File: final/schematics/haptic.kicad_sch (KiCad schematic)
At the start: 11 parts, among them U4 DRV2605LDGST, U5 DRV2605LDGST, U6 DRV2605LDGST

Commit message: fixing issues
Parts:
- C10, C11, C12, C5, C6, C7, C8, C9: footprint (none) -> Capacitor_SMD:C_0603_1608Metric
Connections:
- net +3V3: no longer C10.1, C12.1, C7.1, U4.10 (VDD), U4.5 (EN), U5.10 (VDD), U5.5 (EN), U6.10 (VDD), U6.5 (EN)
- new net +3V3D: C10.1, C12.1, C7.1, U4.10 (VDD), U4.5 (EN), U5.10 (VDD), U5.5 (EN), U6.10 (VDD), U6.5 (EN)

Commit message: finishing
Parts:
- added C39, C41: 10uF, Capacitor_SMD:C_0603_1608Metric, symbol Device:C
- added C40, C42: 0.1uF, Capacitor_SMD:C_0603_1608Metric, symbol Device:C
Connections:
- net +3V3 is gone; now on net +3V3D: C5.1, C6.1
- net +3V3D: now also C39.1, C40.1, C41.1, C42.1
- net DGND: now also C39.2, C40.2, C41.2, C42.2
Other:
- note added: "Decoupling"
- moved on the sheet: C10, C11, C12, C5, C6, C7, C8, C9, U4, U5, U6

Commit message: finished
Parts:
- removed C11, C12: 1uF, Capacitor_SMD:C_0603_1608Metric, symbol Device:C
- removed C41: 10uF, Capacitor_SMD:C_0603_1608Metric, symbol Device:C
- removed C42: 0.1uF, Capacitor_SMD:C_0603_1608Metric, symbol Device:C
- removed U6: DRV2605LDGST, DRV2605LDGST:SOP50P490X110-10N, symbol DRV2605LDGST:DRV2605LDGST
- added R42, R43, R44, R45: 2.2k, Resistor_SMD:R_0603_1608Metric, symbol Device:R
- added R46, R47, R48: 10k, Resistor_SMD:R_0603_1608Metric, symbol Device:R
- added TP17, TP18: TestPoint, Connector_Pin:Pin_D1.0mm_L10.0mm_LooseFit, symbol Connector:TestPoint
- added TP19: MOT1+, Connector_Pin:Pin_D1.1mm_L8.5mm_W2.5mm_FlatFork, symbol Connector:TestPoint
- added TP20: MOT1-, Connector_Pin:Pin_D1.1mm_L8.5mm_W2.5mm_FlatFork, symbol Connector:TestPoint
- added TP21: MOT2+, Connector_Pin:Pin_D1.1mm_L8.5mm_W2.5mm_FlatFork, symbol Connector:TestPoint
- added TP22: MOT2-, Connector_Pin:Pin_D1.1mm_L8.5mm_W2.5mm_FlatFork, symbol Connector:TestPoint
- added U3: TCA9543APWR, TCA9543APWR:IC_TCA9543APWR, symbol TCA9543APWR:TCA9543APWR
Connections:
- net +3V3D: now also R42.2, R43.2, R44.2, R45.2, R46.1, R47.1, R48.1, U3.14 (VCC)
- net DGND: now also U3.1 (A0), U3.2 (A1), U3.7 (GND)
- net MOT1+: now also TP19.1
- net MOT1-: now also TP20.1
- net MOT2+: now also TP21.1
- net MOT2-: now also TP22.1
- net PWM1: now also TP17.1
- net PWM2: now also TP18.1
- net SCL: now also U3.12 (SCL)
- net SDA: now also U3.13 (SDA)
- new net: R46.2, U3.4 (~{INT0})
- new net: R47.2, U3.8 (~{INT1})
- new net: R42.1, U3.10 (SC1)
- new net: R48.2, U3.3 (~{RESET})
- new net: R45.1, U3.5 (SD0)
- new net: R44.1, U3.6 (SC0)
- new net: R43.1, U3.9 (SD1)
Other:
- note removed: "Haptic Driver 3"
- moved on the sheet: C39, C40, C5, C6

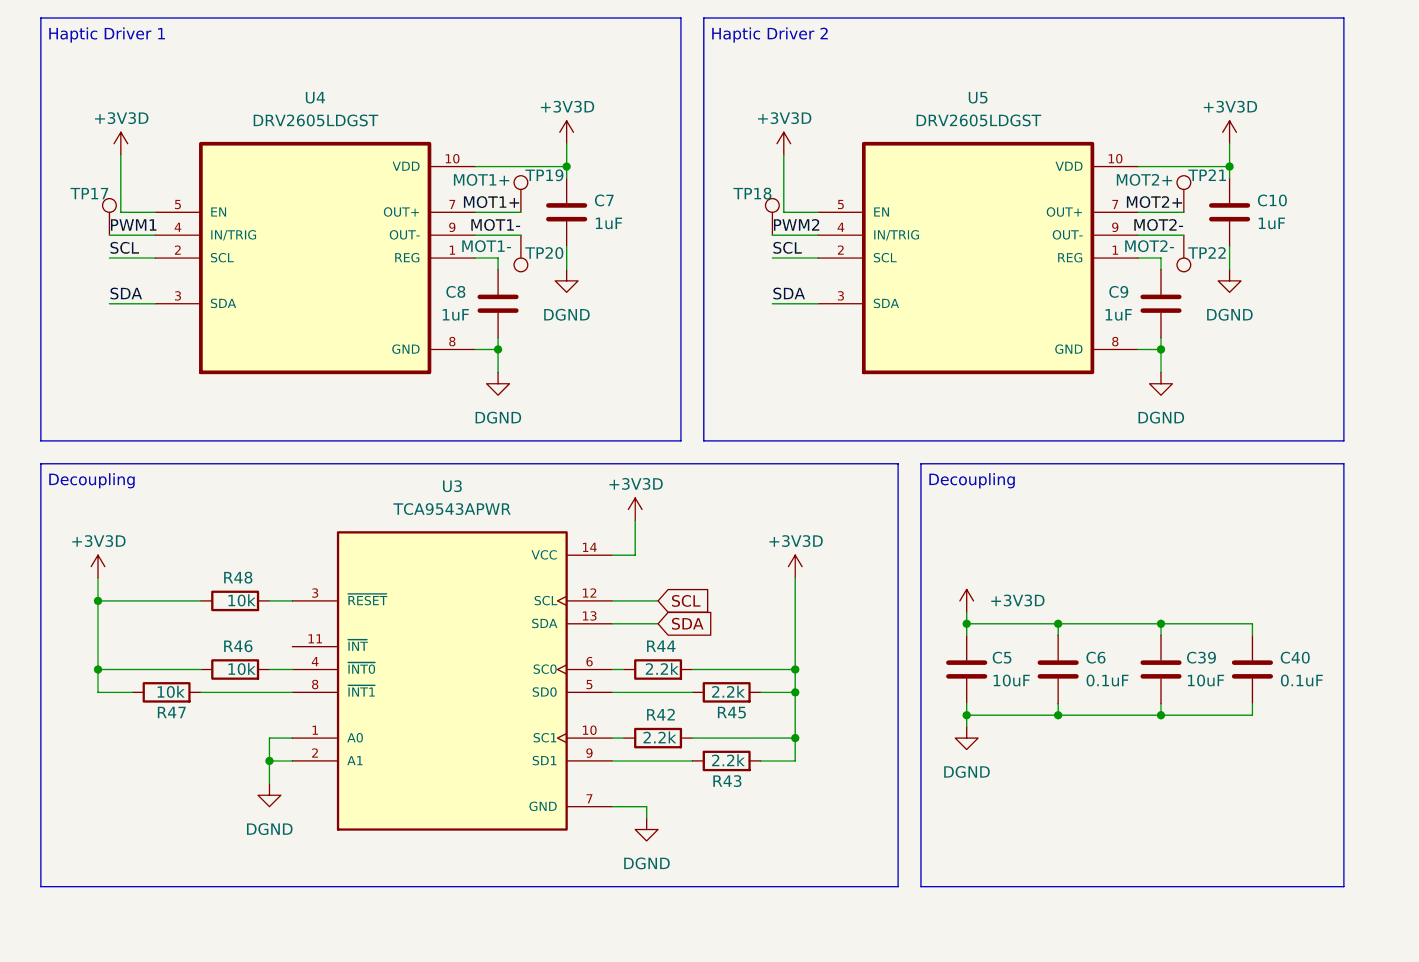
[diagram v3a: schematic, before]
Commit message: fixed jumper connection
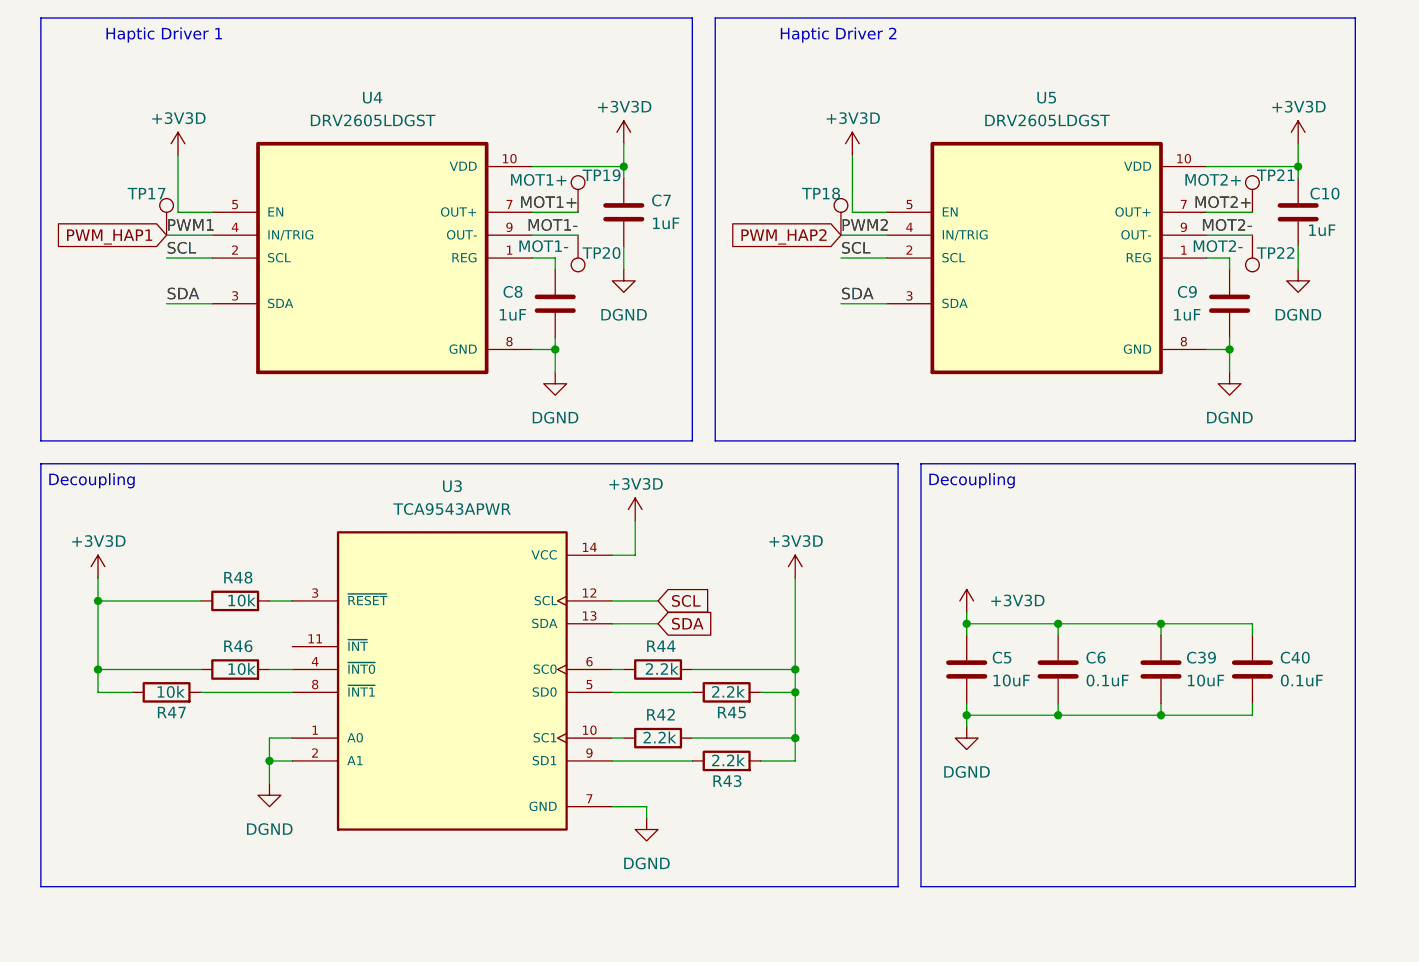
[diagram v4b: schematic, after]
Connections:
- net PWM1 renamed PWM_HAP1
- net PWM2 renamed PWM_HAP2
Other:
- moved on the sheet: C10, C7, C8, C9, TP17, TP18, TP19, TP20, TP21, TP22, U4, U5

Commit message: fixing
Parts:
- removed TP17, TP18: TestPoint, Connector_Pin:Pin_D1.0mm_L10.0mm_LooseFit, symbol Connector:TestPoint
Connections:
- net PWM_HAP1 is gone; now on net DGND: U4.4 (IN/TRIG)
- net PWM_HAP2 is gone; now on net DGND: U5.4 (IN/TRIG)
- net SCL: no longer U4.2 (SCL)
- net SDA: no longer U4.3 (SDA), U5.3 (SDA)
- new net SCL_H1: U4.2 (SCL)
- new net SDA_H1: U4.3 (SDA)
- new net SDA_H2: U5.3 (SDA)
